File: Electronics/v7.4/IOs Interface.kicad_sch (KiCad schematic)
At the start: 29 parts, among them IC1 MC74VHC1GT125, Q2 DMP2035U-7

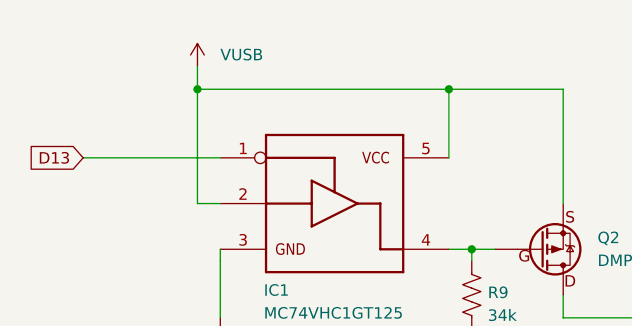
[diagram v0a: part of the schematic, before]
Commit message: Decreased consumption and added STEMMA connector.
- Updated Bat's resistor divider to 0.1% tolerance
- Reduced LEDs' current to bellow 1 mA
- Updated buzzer model
- Increased available voltage to motor
- Added STEMMA (2mm ) connector

To do:
- Update STEMMA to STEMMA QT (2mm)
- (Maybe) Update charging current to slightly bellow 500 mA

Co-Authored-By: David Palma <78764277+davidpalma666@users.noreply.github.com>
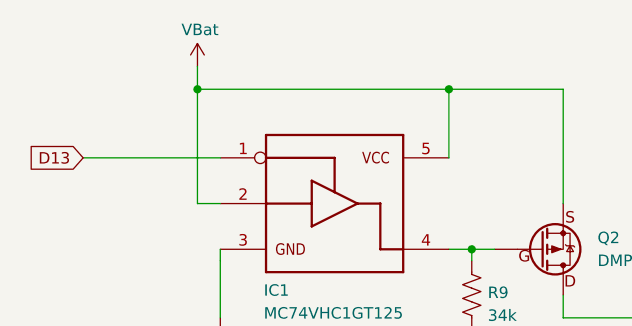
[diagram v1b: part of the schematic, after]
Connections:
- net VUSB renamed VBat
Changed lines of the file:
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@@
 			)
 		)
-		(property "Description" ""
+		(property "Description" "OPTICAL IR sensor (OEPS K01 022A)"
 			(at 46.99 142.24 0)
 			(effects
@@
 			)
 		)
-		(property "Description" ""
+		(property "Description" "RGB Neopixel addressable 5mmx5mm (OEPS K01 012A)"
 			(at 187.96 74.93 0)
 			(effects
@@
 			)
 		)
-		(property "Description" ""
+		(property "Description" "RGB Neopixel addressable 5mmx5mm (OEPS K01 012A)"
 			(at 264.16 74.93 0)
 			(effects
@@
 			)
 		)
-		(property "Description" "Unpolarized capacitor, small symbol"
+		(property "Description" "SMD CER 0402 1uF 25V ±10% X5R"
 			(at 130.81 35.56 0)
 			(effects
@@
 			)
 		)
-		(property "Description" "Buzzer, polarized"
+		(property "Description" "BUZZER PIEZO 3V 12.2MM (OEPS K01 014)"
 			(at 91.44 180.34 0)
 			(effects
@@
 			)
 		)
-		(property "Description" ""
+		(property "Description" "SMD 0402 1kΩ ±1% 0.100W"
 			(at 52.07 121.92 0)
 			(effects
@@
 	)
 	(symbol
-		(lib_id "FED3 SymbLib:VUSB")
-		(at 35.56 24.13 0)
-		(unit 1)
-		(exclude_from_sim no)
-		(in_bom yes)
-		(on_board yes)
-		(dnp no)
-		(fields_autoplaced yes)
-		(property "Reference" "#PWR08"
-			(at 35.56 27.94 0)
-			(effects
-				(font
-					(size 1.27 1.27)
-				)
-				(justify bottom)
-				(hide yes)
-			)
-		)
-		(property "Value" "VUSB"
-			(at 38.1 22.8599 0)
-			(effects
-				(font
-					(size 1.27 1.27)
-				)
-				(justify left)
-			)
-		)
-		(property "Footprint" ""
-			(at 35.56 24.13 0)
-			(effects
-				(font
-					(size 1.27 1.27)
-				)
-				(hide yes)
-			)
-		)
-		(property "Datasheet" ""
-			(at 35.56 24.13 0)
-			(effects
-				(font
-					(size 1.27 1.27)
-				)
-				(hide yes)
-			)
-		)
-		(property "Description" "Power symbol creates a global label with name \"VUSB\""
-			(at 35.56 24.13 0)
-			(effects
-				(font
-					(size 1.27 1.27)
-				)
-				(hide yes)
-			)
-		)
-		(pin "1"
-		)
-		(instances
-			(project "FED3_v7.3"
-				(path "/2ba63f12-2fcd-4471-9636-2762cde37de8/91f92fff-cc86-4ce2-a671-c31760f8020c"
-					(reference "#PWR08")
-					(unit 1)
-				)
-			)
-		)
-	)
-	(symbol
 		(lib_id "power:GNDD")
 		(at 161.29 39.37 0)
@@
 			)
 		)
-		(property "Description" "Unpolarized capacitor, small symbol"
+		(property "Description" "SMD CER 0402 1uF 25V ±10% X5R"
 			(at 168.91 35.56 0)
 			(effects
@@
 			)
 		)
-		(property "Description" ""
+		(property "Description" "RGB Neopixel addressable 5mmx5mm (OEPS K01 012A)"
 			(at 238.76 74.93 0)
 			(effects
@@
 	)
 	(symbol
+		(lib_id "FED3 SymbLib:V_Batt")
+		(at 35.56 24.13 0)
+		(unit 1)
+		(exclude_from_sim no)
+		(in_bom yes)
+		(on_board yes)
+		(dnp no)
+		(property "Reference" "#PWR07"
+			(at 35.56 27.94 0)
+			(effects
+				(font
+					(size 1.27 1.27)
+				)
+				(justify bottom)
+				(hide yes)
+			)
+		)
+		(property "Value" "VBat"
+			(at 33.782 20.066 0)
+			(effects
+				(font
+					(size 1.27 1.27)
+				)
+				(justify left)
+			)
+		)
+		(property "Footprint" ""
+			(at 35.56 24.13 0)
+			(effects
+				(font
+					(size 1.27 1.27)
+				)
+				(hide yes)
+			)
+		)
+		(property "Datasheet" ""
+			(at 35.56 24.13 0)
+			(effects
+				(font
+					(size 1.27 1.27)
+				)
+				(hide yes)
+			)
+		)
+		(property "Description" "Power symbol creates a global label with name \"V_Batt\""
+			(at 35.56 24.13 0)
+			(effects
+				(font
+					(size 1.27 1.27)
+				)
+				(hide yes)
+			)
+		)
+		(pin "1"
+		)
+		(instances
+			(project "FED3"
+				(path "/2ba63f12-2fcd-4471-9636-2762cde37de8/91f92fff-cc86-4ce2-a671-c31760f8020c"
+					(reference "#PWR07")
+					(unit 1)
+				)
+			)
+		)
+	)
+	(symbol
 		(lib_id "Device:R_US")
 		(at 146.05 121.92 0)
@@
 			)
 		)
-		(property "Description" ""
+		(property "Description" "SMD 0402 1kΩ ±1% 0.100W"
 			(at 146.05 121.92 0)
 			(effects
@@
 			)
 		)
-		(property "Description" "Unpolarized capacitor, small symbol"
+		(property "Description" "SMD CER 0402 1uF 25V ±10% X5R"
 			(at 161.29 35.56 0)
 			(effects
@@
 			)
 		)
-		(property "Description" ""
+		(property "Description" "OPTICAL IR sensor (OEPS K01 022A)"
 			(at 91.44 142.24 0)
 			(effects
@@
 			)
 		)
-		(property "Description" ""
+		(property "Description" "SMD 0402 1kΩ ±1% 0.100W"
 			(at 96.52 121.92 0)
 			(effects
@@
 			)
 		)
-		(property "Description" ""
+		(property "Description" "OPTICAL IR sensor (OEPS K01 022A)"
 			(at 140.97 142.24 0)
 			(effects
@@
 			)
 		)
-		(property "Description" "Unpolarized capacitor, small symbol"
+		(property "Description" "SMD CER 0402 1uF 25V ±10% X5R"
 			(at 138.43 35.56 0)
 			(effects
@@
 			)
 		)
-		(property "Description" ""
+		(property "Description" "RGB Neopixel addressable 5mmx5mm (OEPS K01 012A)"
 			(at 86.36 74.93 0)
 			(effects
@@
 			)
 		)
-		(property "Description" ""
+		(property "Description" "RGB Neopixel addressable 5mmx5mm (OEPS K01 012A)"
 			(at 238.76 114.3 0)
 			(effects
@@
 			)
 		)
-		(property "Description" ""
+		(property "Description" "RGB Neopixel addressable 5mmx5mm (OEPS K01 012A)"
 			(at 137.16 74.93 0)
 			(effects
@@
 			)
 		)
-		(property "Description" ""
+		(property "Description" "SMD 0402 34kΩ ±0.1% 0.063W"
 			(at 66.04 49.53 0)
 			(effects
@@
 			)
 		)
-		(property "Description" ""
+		(property "Description" "RGB Neopixel addressable 5mmx5mm (OEPS K01 012A)"
 			(at 111.76 74.93 0)
 			(effects
@@
 			)
 		)
-		(property "Description" ""
+		(property "Description" "RGB Neopixel addressable 5mmx5mm (OEPS K01 012A)"
 			(at 264.16 114.3 0)
 			(effects
@@
 			)
 		)
-		(property "Description" "Unpolarized capacitor, small symbol"
+		(property "Description" "SMD CER 0402 1uF 25V ±10% X5R"
 			(at 153.67 35.56 0)
 			(effects
@@
 			)
 		)
-		(property "Description" ""
+		(property "Description" "RGB Neopixel addressable 5mmx5mm (OEPS K01 012A)"
 			(at 162.56 74.93 0)
 			(effects
@@
 			)
 		)
-		(property "Description" ""
+		(property "Description" "3.5MM JACK STEREO 90º"
 			(at 46.99 180.34 0)
 			(effects
@@
 			)
 		)
-		(property "Description" "Unpolarized capacitor, small symbol"
+		(property "Description" "SMD CER 0402 1uF 25V ±10% X5R"
 			(at 146.05 35.56 0)
 			(effects
@@
 			)
 		)
-		(property "Description" ""
+		(property "Description" "DC DC CONVERTER Boost/Inverter 2output ±40V 1.3A"
 			(at 50.8 39.37 0)
 			(effects
@@
 			)
 		)
-		(property "Description" ""
+		(property "Description" "SMD 0402 330Ω ±1% 0.063W"
 			(at 67.31 77.47 0)
 			(effects
@@
 			)
 		)
-		(property "Description" ""
+		(property "Description" "RGB Neopixel addressable 5mmx5mm (OEPS K01 012A)"
 			(at 213.36 74.93 0)
 			(effects

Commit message: Added schematic sheet
- Fixed some typos
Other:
- company: (none) -> Kravitz Lab
- title: (none) -> FED3 Control Board
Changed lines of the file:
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@@
 	(generator_version "9.0")
 	(paper "A4")
+	(title_block
+		(title "FED3 Control Board")
+		(rev "7.4")
+		(company "Kravitz Lab")
+		(comment 1 "Open Ephys, Inc.")
+	)
 	(junction
 		(at 142.24 52.07)

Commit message: Prepared files for production.
Also fixed #13
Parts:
- LED1, LED10, LED2, LED3, LED4, LED5, LED6, LED7, LED8, LED9: MPN SK6812RGBW-BW -> XT1511RGBW-BW
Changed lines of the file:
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@@
 			)
 		)
-		(property "MPN" "SK6812RGBW-BW"
+		(property "MPN" "XT1511RGBW-BW"
 			(at 187.96 74.93 0)
 			(effects
@@
 			)
 		)
-		(property "MPN" "SK6812RGBW-BW"
+		(property "MPN" "XT1511RGBW-BW"
 			(at 264.16 74.93 0)
 			(effects
@@
 			)
 		)
-		(property "MPN" "SK6812RGBW-BW"
+		(property "MPN" "XT1511RGBW-BW"
 			(at 238.76 74.93 0)
 			(effects
@@
 			)
 		)
-		(property "MPN" "SK6812RGBW-BW"
+		(property "MPN" "XT1511RGBW-BW"
 			(at 86.36 74.93 0)
 			(effects
@@
 			)
 		)
-		(property "MPN" "SK6812RGBW-BW"
+		(property "MPN" "XT1511RGBW-BW"
 			(at 238.76 114.3 0)
 			(effects
@@
 			)
 		)
-		(property "MPN" "SK6812RGBW-BW"
+		(property "MPN" "XT1511RGBW-BW"
 			(at 137.16 74.93 0)
 			(effects
@@
 			)
 		)
-		(property "MPN" "SK6812RGBW-BW"
+		(property "MPN" "XT1511RGBW-BW"
 			(at 111.76 74.93 0)
 			(effects
@@
 			)
 		)
-		(property "MPN" "SK6812RGBW-BW"
+		(property "MPN" "XT1511RGBW-BW"
 			(at 264.16 114.3 0)
 			(effects
@@
 			)
 		)
-		(property "MPN" "SK6812RGBW-BW"
+		(property "MPN" "XT1511RGBW-BW"
 			(at 162.56 74.93 0)
 			(effects
@@
 			)
 		)
-		(property "Description" "DC DC CONVERTER Boost/Inverter 2output ±40V 1.3A"
+		(property "Description" "BUFFER NON-INVERT 1CH 3-STATE"
 			(at 50.8 39.37 0)
 			(effects
@@
 			)
 		)
-		(property "MPN" "SK6812RGBW-BW"
+		(property "MPN" "XT1511RGBW-BW"
 			(at 213.36 74.93 0)
 			(effects
